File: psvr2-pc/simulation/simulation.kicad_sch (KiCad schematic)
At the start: 29 parts, among them Q1 PMOS, Q2 PMOS, Q3 NPN, Q4 PMOS, Q5 PMOS, Q6 NPN, Q8 PMOS

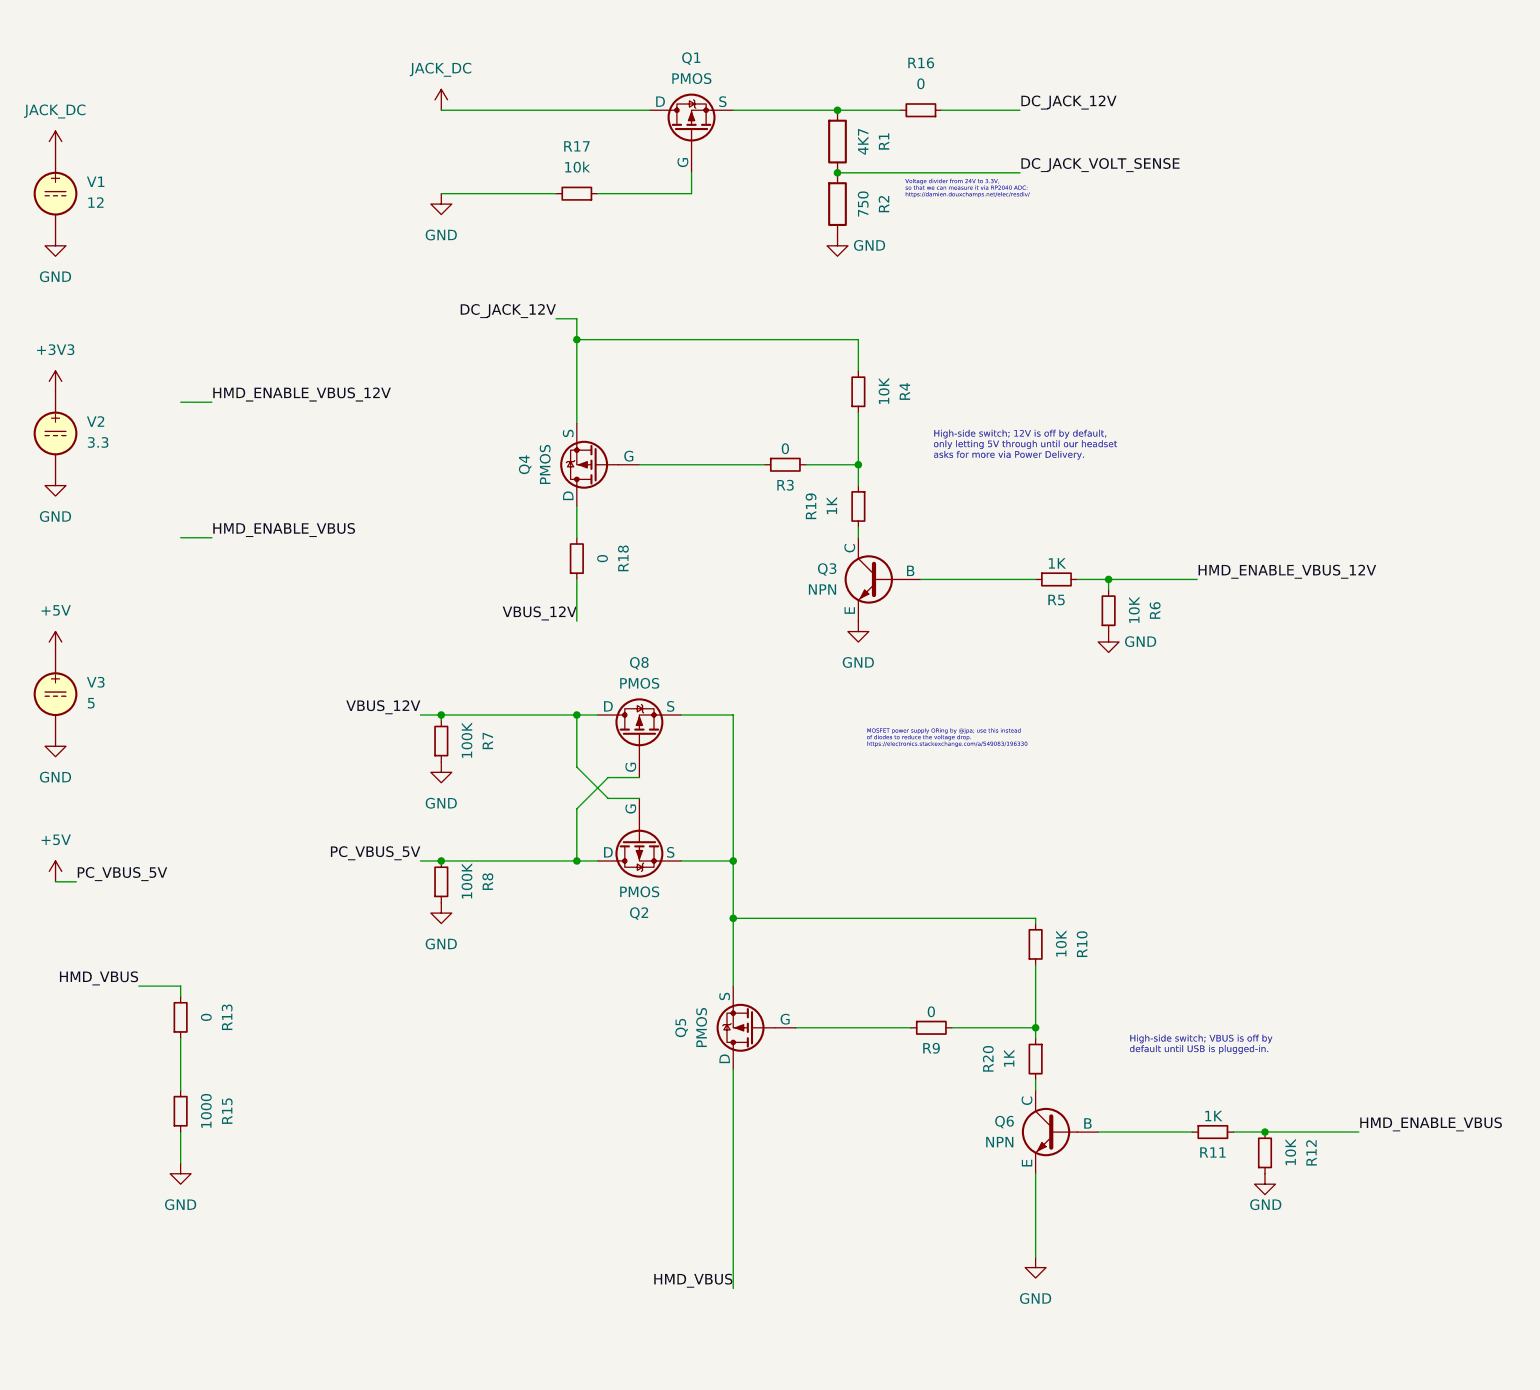
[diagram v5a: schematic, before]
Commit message: Now the simulation works again after changing the component and doing other stuff I don't understand. Raise the NPN resistor from 1K to 7K ohms to reduce the gate-source voltage difference and avoid issues.
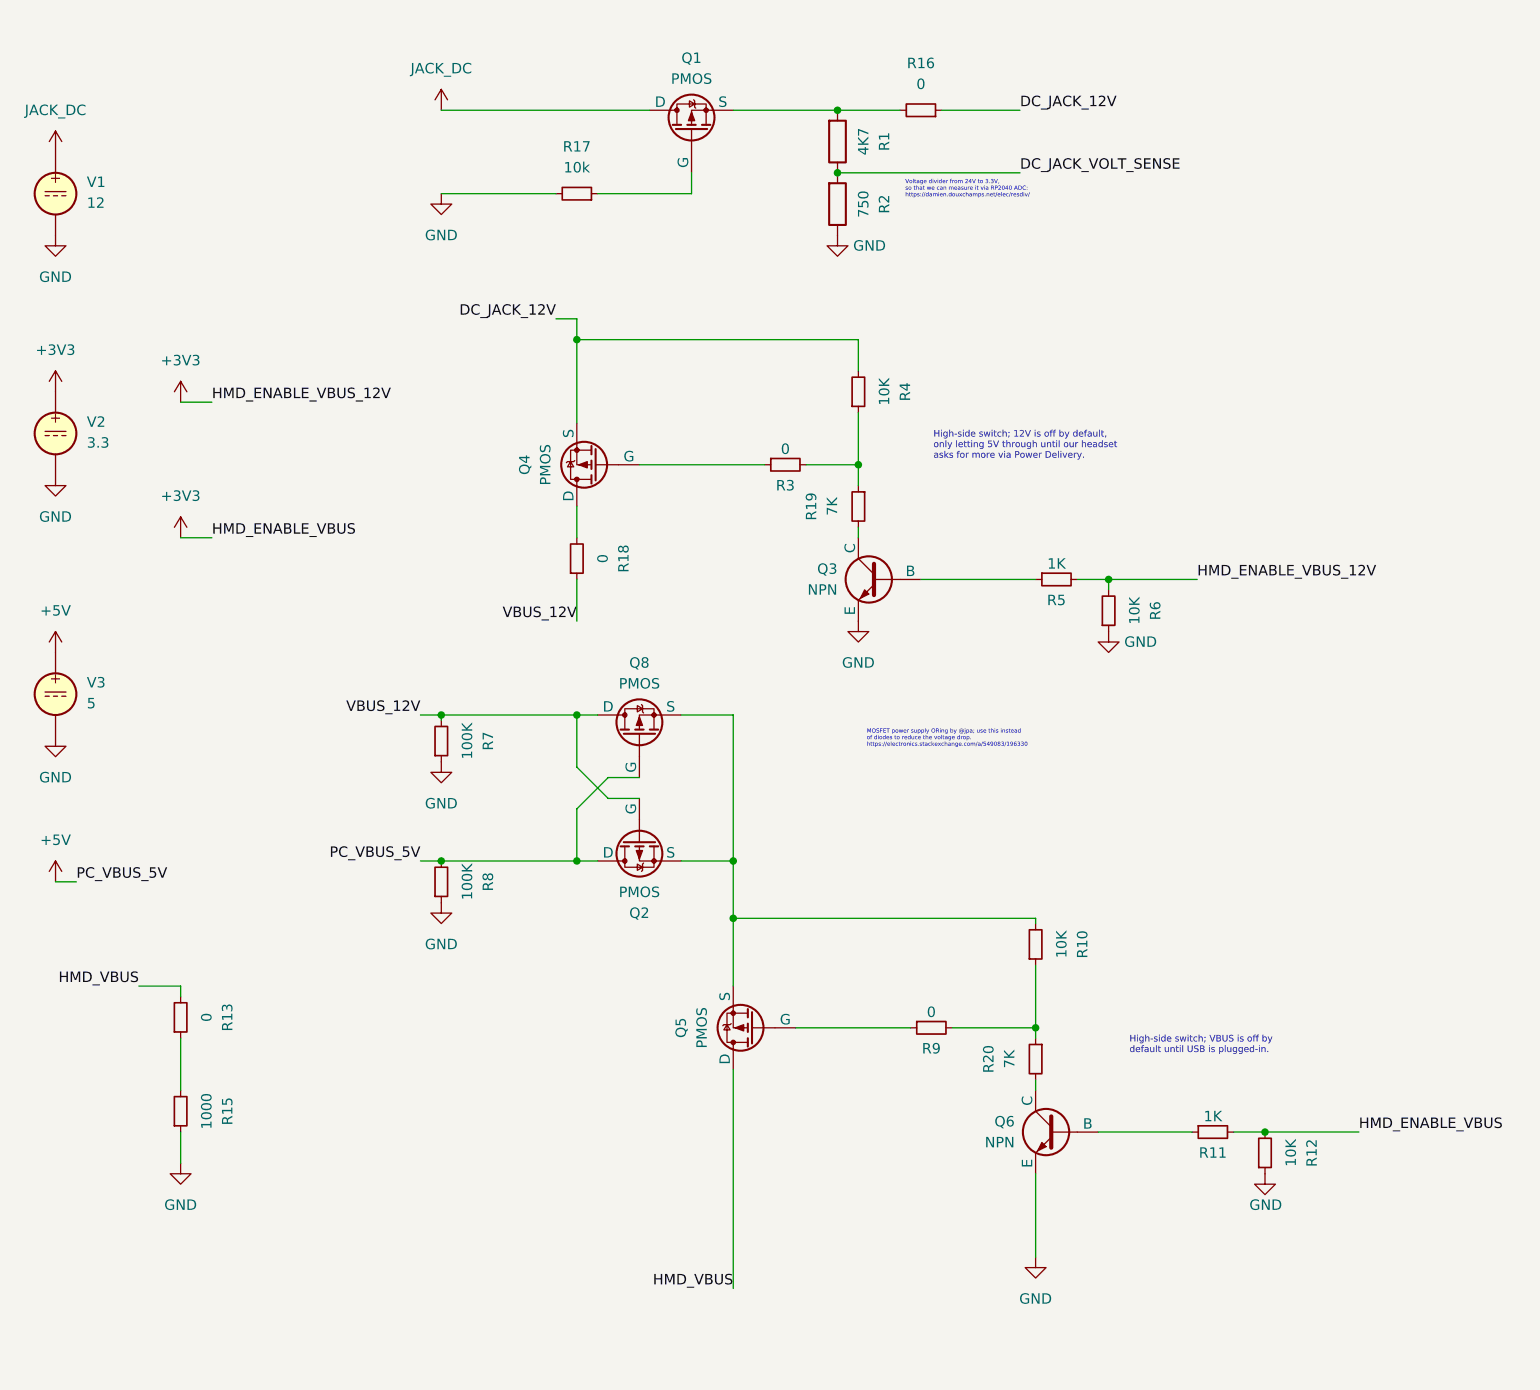
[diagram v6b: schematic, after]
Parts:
- R19, R20: value 1K -> 7K
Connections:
- net HMD_ENABLE_VBUS is gone; now on net +3V3: R11.2, R12.2
- net HMD_ENABLE_VBUS_12V is gone; now on net +3V3: R5.2, R6.2
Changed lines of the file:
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@@
+	)
+	(symbol
+		(lib_id "Simulation_SPICE:NPN")
+		(at 143.51 146.05 0)
+		(mirror y)
+		(unit 1)
+		(exclude_from_sim no)
+		(in_bom yes)
+		(on_board yes)
+		(dnp no)
+		(fields_autoplaced yes)
+		(property "Reference" "Q6"
+			(at 138.43 144.7799 0)
+			(effects
+				(font
+					(size 1.27 1.27)
+				)
+				(justify left)
+			)
+		)
+		(property "Value" "NPN"
+			(at 138.43 147.3199 0)
+			(effects
+				(font
+					(size 1.27 1.27)
+				)
+				(justify left)
+			)
+		)
+		(property "Footprint" ""
+			(at 80.01 146.05 0)
+			(effects
+				(font
+					(size 1.27 1.27)
+				)
+				(hide yes)
+			)
+		)
+		(property "Datasheet" "https://ngspice.sourceforge.io/docs/ngspice-html-manual/manual.xhtml#cha_BJTs"
+			(at 80.01 146.05 0)
+			(effects
+				(font
+					(size 1.27 1.27)
+				)
+				(hide yes)
+			)
+		)
+		(property "Description" "Bipolar transistor symbol for simulation only, substrate tied to the emitter"
+			(at 143.51 146.05 0)
+			(effects
+				(font
+					(size 1.27 1.27)
+				)
+				(hide yes)
+			)
+		)
+		(property "Sim.Device" "NPN"
+			(at 143.51 146.05 0)
+			(effects
+				(font
+					(size 1.27 1.27)
+				)
+				(hide yes)
+			)
+		)
+		(property "Sim.Type" "GUMMELPOON"
+			(at 143.51 146.05 0)
+			(effects
+				(font
+					(size 1.27 1.27)
+				)
+				(hide yes)
+			)
+		)
+		(property "Sim.Pins" "1=C 2=B 3=E"
+			(at 143.51 146.05 0)
+			(effects
+				(font
+					(size 1.27 1.27)
+				)
+				(hide yes)
+			)
+		)
+		(pin "1"
+		)
+		(pin "3"
+		)
+		(pin "2"
+		)
+		(instances
+			(project "simulation"
+				(path "/f11bb3d3-5794-4a95-b9a9-d0bd9f1c0d65"
+					(reference "Q6")
+					(unit 1)
+				)
+			)
+		)
 	)
 	(symbol
@@
 	)
 	(symbol
+		(lib_id "power:+3V3")
+		(at 36.83 57.15 0)
+		(unit 1)
+		(exclude_from_sim no)
+		(in_bom yes)
+		(on_board yes)
+		(dnp no)
+		(fields_autoplaced yes)
+		(property "Reference" "#PWR08"
+			(at 36.83 60.96 0)
+			(effects
+				(font
+					(size 1.27 1.27)
+				)
+				(hide yes)
+			)
+		)
+		(property "Value" "+3V3"
+			(at 36.83 52.07 0)
+			(effects
+				(font
+					(size 1.27 1.27)
+				)
+			)
+		)
+		(property "Footprint" ""
+			(at 36.83 57.15 0)
+			(effects
+				(font
+					(size 1.27 1.27)
+				)
+				(hide yes)
+			)
+		)
+		(property "Datasheet" ""
+			(at 36.83 57.15 0)
+			(effects
+				(font
+					(size 1.27 1.27)
+				)
+				(hide yes)
+			)
+		)
+		(property "Description" "Power symbol creates a global label with name \"+3V3\""
+			(at 36.83 57.15 0)
+			(effects
+				(font
+					(size 1.27 1.27)
+				)
+				(hide yes)
+			)
+		)
+		(pin "1"
+		)
+		(instances
+			(project "simulation"
+				(path "/f11bb3d3-5794-4a95-b9a9-d0bd9f1c0d65"
+					(reference "#PWR08")
+					(unit 1)
+				)
+			)
+		)
+	)
+	(symbol
 		(lib_id "Device:R_Small")
 		(at 128.27 133.35 90)
@@
 	)
 	(symbol
-		(lib_id "Simulation_SPICE:NPN")
-		(at 143.51 146.05 0)
-		(mirror y)
-		(unit 1)
-		(exclude_from_sim no)
-		(in_bom yes)
-		(on_board yes)
-		(dnp no)
-		(fields_autoplaced yes)
-		(property "Reference" "Q6"
-			(at 138.43 144.7799 0)
-			(effects
-				(font
-					(size 1.27 1.27)
-				)
-				(justify left)
-			)
-		)
-		(property "Value" "NPN"
-			(at 138.43 147.3199 0)
-			(effects
-				(font
-					(size 1.27 1.27)
-				)
-				(justify left)
-			)
-		)
-		(property "Footprint" ""
-			(at 80.01 146.05 0)
-			(effects
-				(font
-					(size 1.27 1.27)
-				)
-				(hide yes)
-			)
-		)
-		(property "Datasheet" "https://ngspice.sourceforge.io/docs/ngspice-html-manual/manual.xhtml#cha_BJTs"
-			(at 80.01 146.05 0)
-			(effects
-				(font
-					(size 1.27 1.27)
-				)
-				(hide yes)
-			)
-		)
-		(property "Description" "Bipolar transistor symbol for simulation only, substrate tied to the emitter"
-			(at 143.51 146.05 0)
-			(effects
-				(font
-					(size 1.27 1.27)
-				)
-				(hide yes)
-			)
-		)
-		(property "Sim.Device" "SUBCKT"
-			(at 143.51 146.05 0)
-			(effects
-				(font
-					(size 1.27 1.27)
-				)
-				(hide yes)
-			)
-		)
-		(property "Sim.Pins" "1=D 2=G 3=S"
-			(at 143.51 146.05 0)
-			(effects
-				(font
-					(size 1.27 1.27)
-				)
-				(hide yes)
-			)
-		)
-		(property "Sim.Library" "C:\\Users\\Usuario\\Downloads\\si2301cds_ps_revb\\si2301cds_ps Rev B.lib"
-			(at 143.51 146.05 0)
-			(effects
-				(font
-					(size 1.27 1.27)
-				)
-				(hide yes)
-			)
-		)
-		(property "Sim.Name" "Si2301CDS"
-			(at 143.51 146.05 0)
-			(effects
-				(font
-					(size 1.27 1.27)
-				)
-				(hide yes)
-			)
-		)
-		(pin "1"
-		)
-		(pin "3"
-		)
-		(pin "2"
-		)
-		(instances
-			(project "simulation"
-				(path "/f11bb3d3-5794-4a95-b9a9-d0bd9f1c0d65"
-					(reference "Q6")
-					(unit 1)
-				)
-			)
-		)
-	)
-	(symbol
 		(lib_id "power:GND")
 		(at 119.38 83.82 0)
@@
 			)
 		)
-		(property "Value" "1K"
+		(property "Value" "7K"
 			(at 137.795 137.16 90)
 			(effects
@@
 	)
 	(symbol
+		(lib_id "power:+3V3")
+		(at 36.83 73.66 0)
+		(unit 1)
+		(exclude_from_sim no)
+		(in_bom yes)
+		(on_board yes)
+		(dnp no)
+		(fields_autoplaced yes)
+		(property "Reference" "#PWR017"
+			(at 36.83 77.47 0)
+			(effects
+				(font
+					(size 1.27 1.27)
+				)
+				(hide yes)
+			)
+		)
+		(property "Value" "+3V3"
+			(at 36.83 68.58 0)
+			(effects
+				(font
+					(size 1.27 1.27)
+				)
+			)
+		)
+		(property "Footprint" ""
+			(at 36.83 73.66 0)
+			(effects
+				(font
+					(size 1.27 1.27)
+				)
+				(hide yes)
+			)
+		)
+		(property "Datasheet" ""
+			(at 36.83 73.66 0)
+			(effects
+				(font
+					(size 1.27 1.27)
+				)
+				(hide yes)
+			)
+		)
+		(property "Description" "Power symbol creates a global label with name \"+3V3\""
+			(at 36.83 73.66 0)
+			(effects
+				(font
+					(size 1.27 1.27)
+				)
+				(hide yes)
+			)
+		)
+		(pin "1"
+		)
+		(instances
+			(project "simulation"
+				(path "/f11bb3d3-5794-4a95-b9a9-d0bd9f1c0d65"
+					(reference "#PWR017")
+					(unit 1)
+				)
+			)
+		)
+	)
+	(symbol
 		(lib_id "Device:R_Small")
 		(at 127 21.59 270)
@@
 			)
 		)
-		(property "Value" "1K"
+		(property "Value" "7K"
 			(at 116.205 69.85 90)
 			(effects

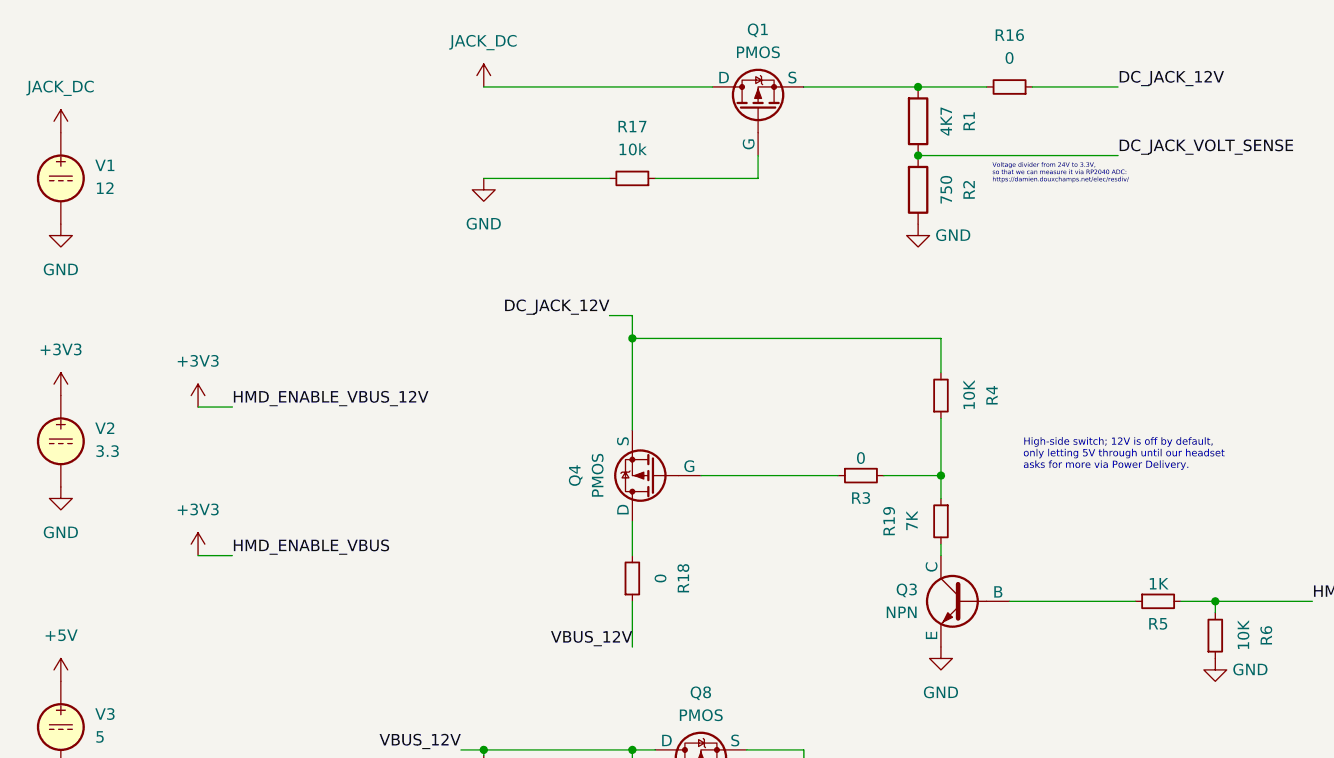
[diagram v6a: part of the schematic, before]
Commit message: Add a resistor voltage divider in the reverse voltage protection simulation to protect the gate and avoid Vgs (gate-source pin difference)
getting too big and burning the MOSFET, usually the Vds limit (-30V) is bigger than the Vgs one (here ±12V):
That way we can withstand until 30V, in theory.

https://electronics.stackexchange.com/a/61699/196330
https://aosmd.com/sites/default/files/res/datasheets/AO3401A.pdf
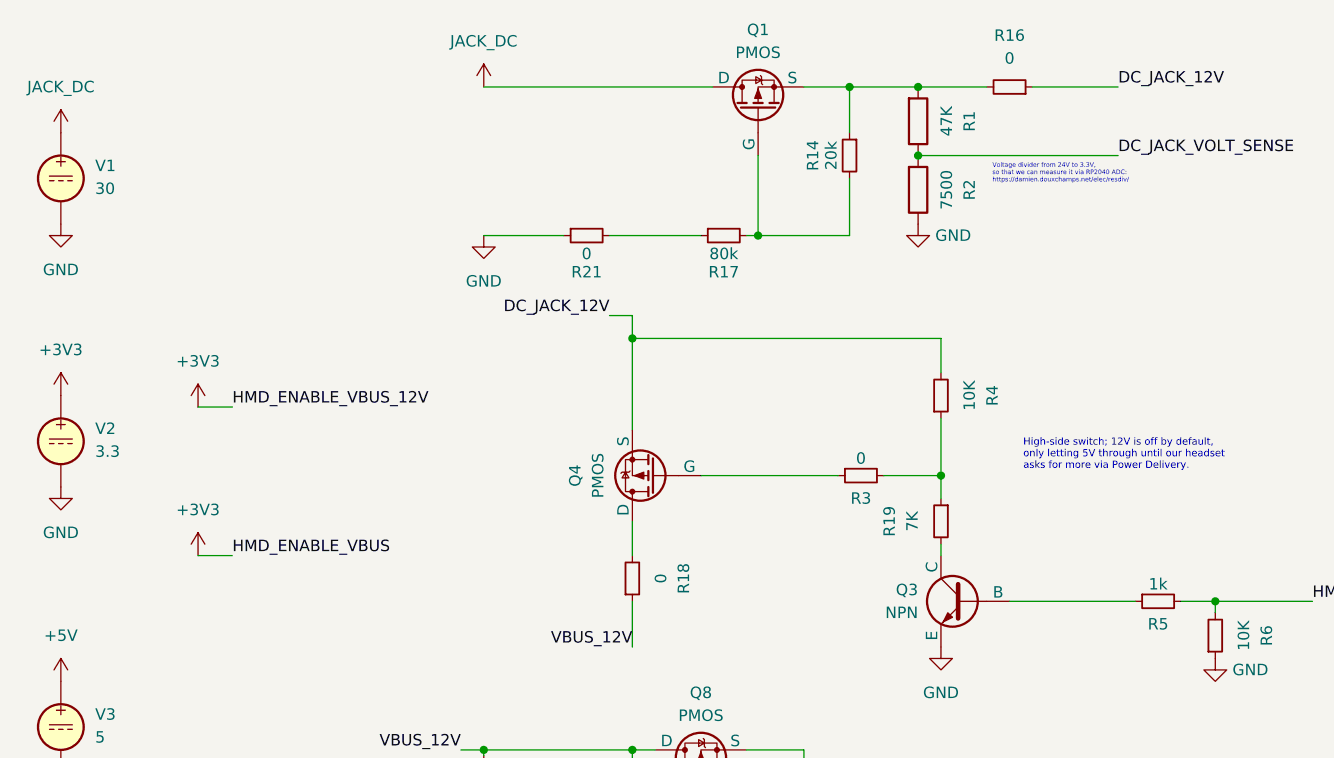
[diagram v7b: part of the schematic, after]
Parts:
- added R14: 20k, Resistor_SMD:R_0805_2012Metric, symbol Device:R_Small
- added R21: 0, Resistor_SMD:R_0805_2012Metric, symbol Device:R_Small
- R1: value 4K7 -> 47K
- R17: value 10k -> 80k
- R2: value 750 -> 7500
- R5: value 1K -> 1k
- V1: value 12 -> 30
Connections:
- net GND: now also R21.1; no longer R17.2
- net at Q1.3 (S), R1.2, R16.2: now also R14.1
- net at Q1.2 (G): now also R17.2, R14.2; no longer R17.1
- new net: R17.1, R21.2
